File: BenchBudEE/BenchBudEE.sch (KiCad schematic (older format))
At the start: 0 parts

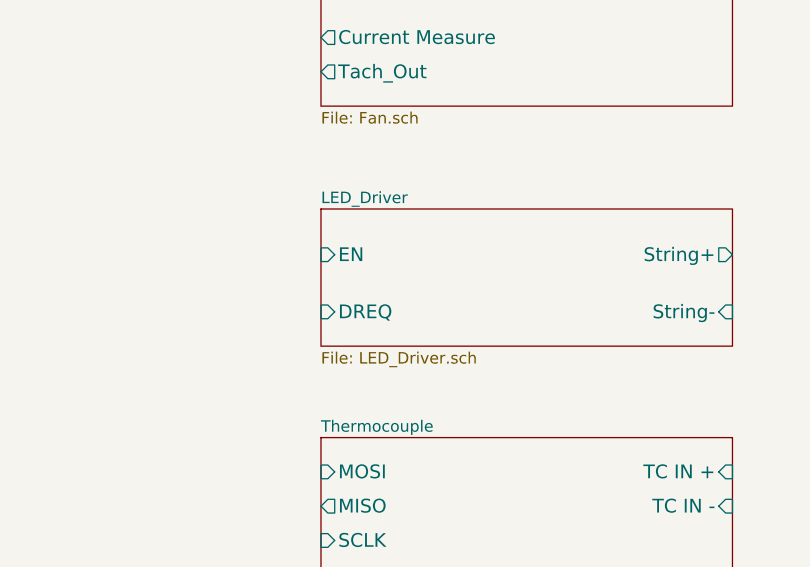
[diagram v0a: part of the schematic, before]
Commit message: Populated the LED Driver block based on the AP5726.
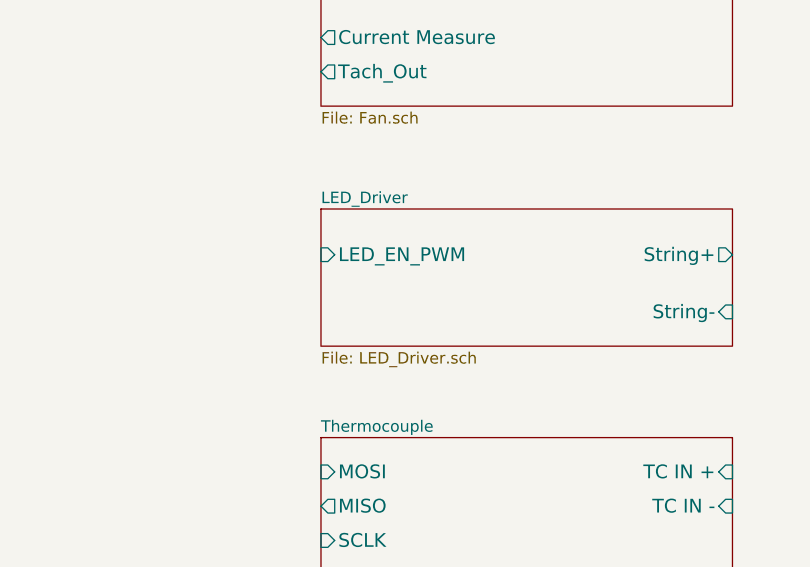
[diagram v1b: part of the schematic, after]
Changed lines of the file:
@@
 Sheet 1 9
 Title ""
-Date "9 feb 2014"
+Date "10 feb 2014"
 Rev ""
 Comp ""
@@
 F0 "LED_Driver" 50
 F1 "LED_Driver.sch" 50
-F2 "EN" I L 7850 4250 60
-F3 "DREQ" I L 7850 4500 60
-F4 "String+" O R 9650 4250 60
-F5 "String-" I R 9650 4500 60
+F2 "String+" O R 9650 4250 60
+F3 "String-" I R 9650 4500 60
+F4 "LED_EN_PWM" I L 7850 4250 60
 $EndSheet
 $Sheet

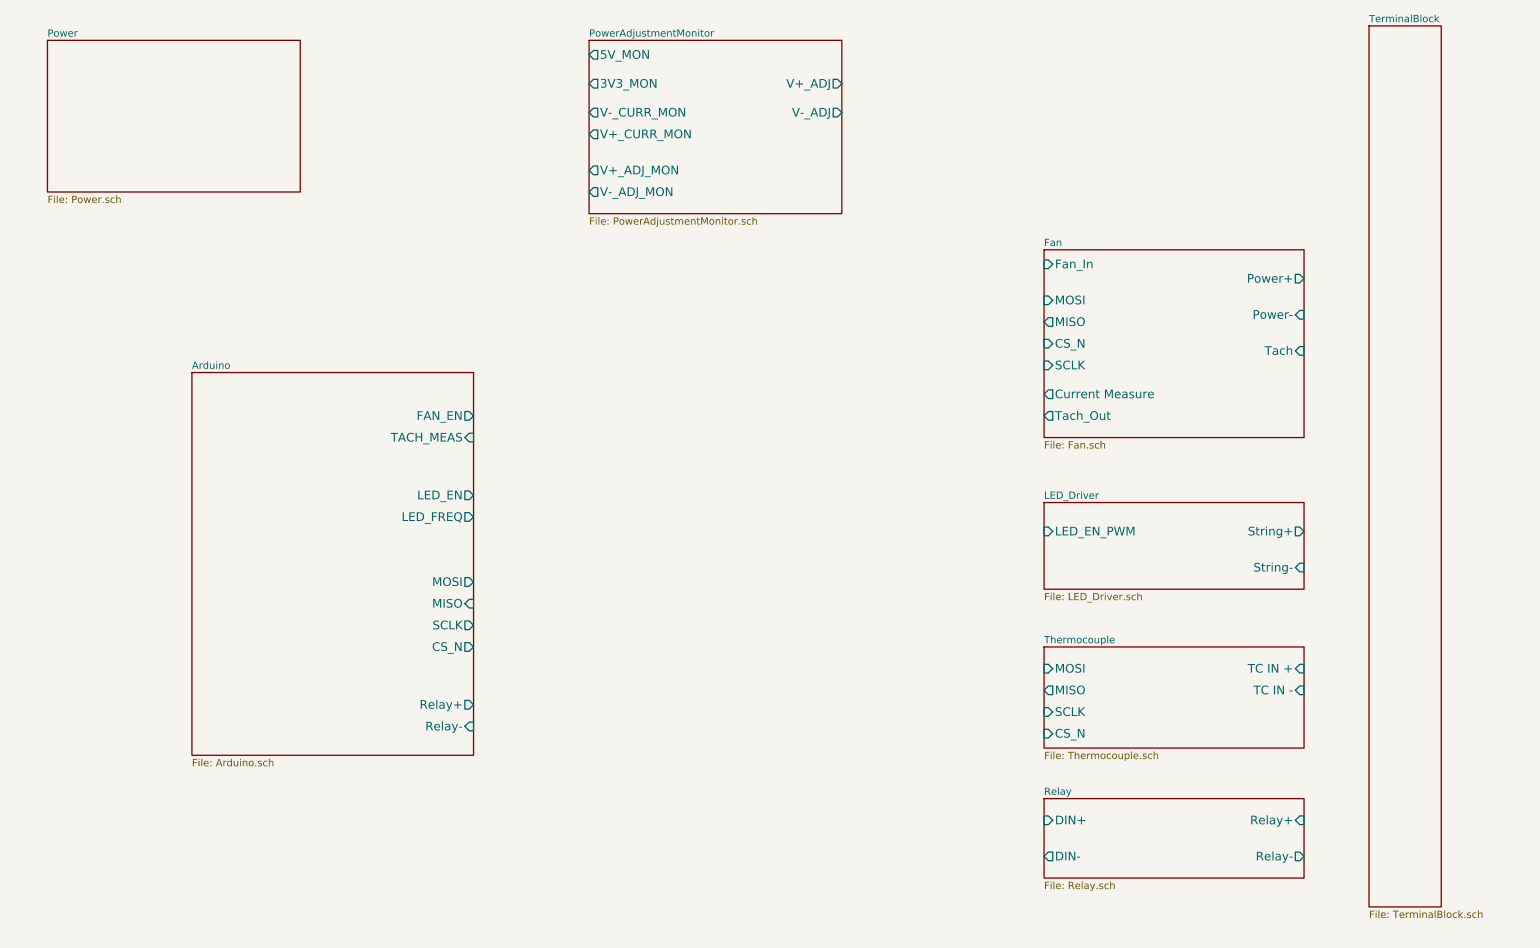
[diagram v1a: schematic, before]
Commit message: Populated the Arduino block and top level wiring.
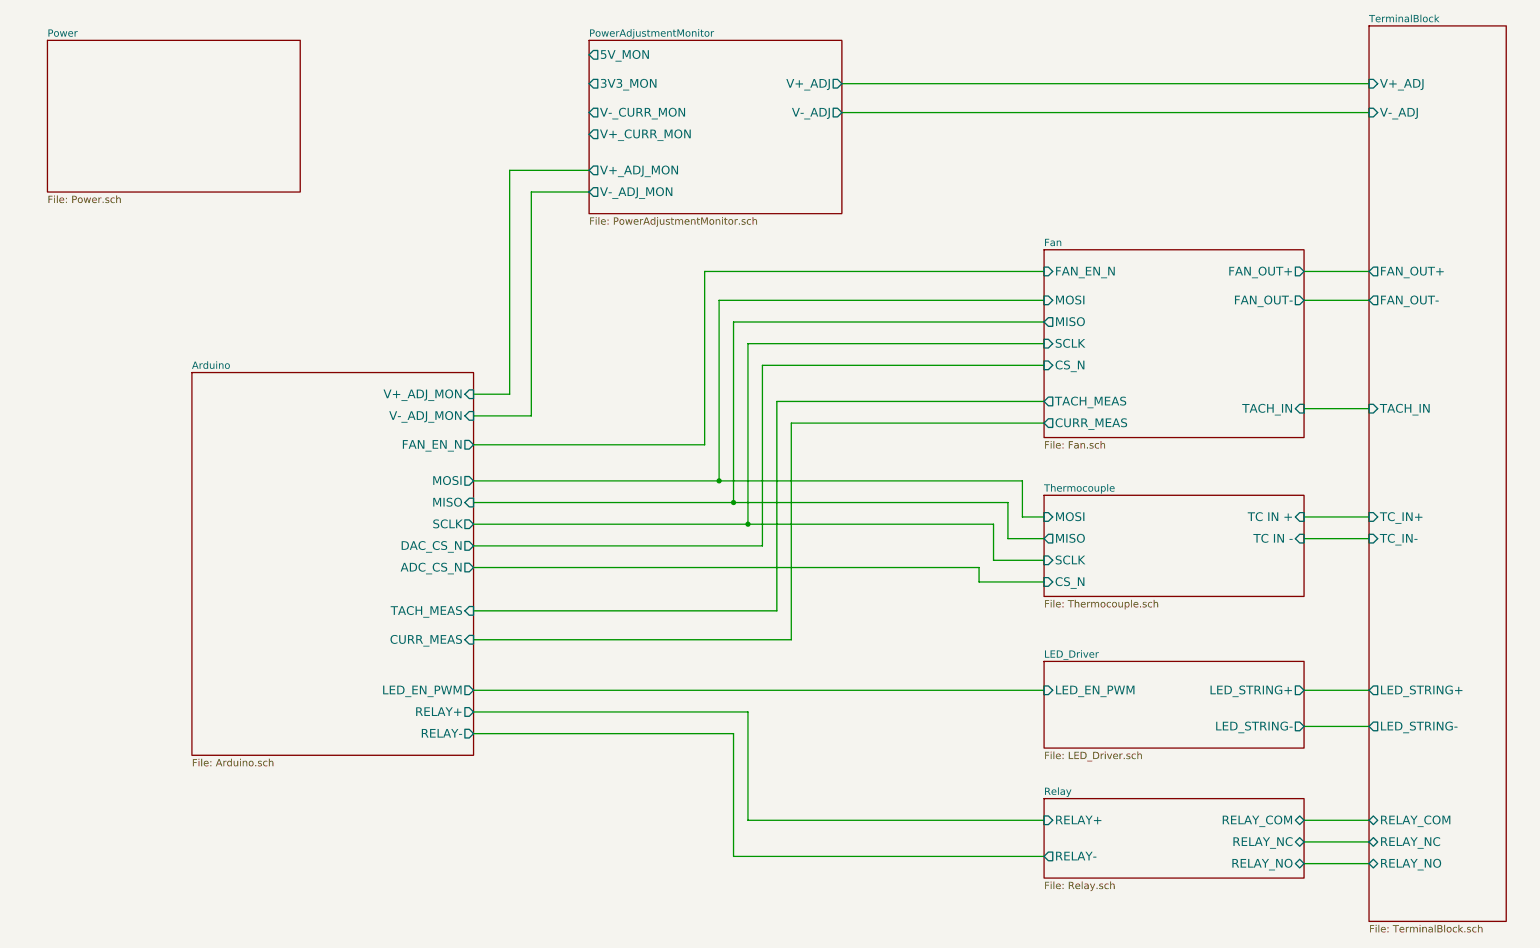
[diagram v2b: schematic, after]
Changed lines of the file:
@@
 $EndDescr
 $Sheet
-S 1950 3150 1950 2650
-U 52EC4D59
-F0 "Arduino" 50
-F1 "Arduino.sch" 50
-F2 "Relay+" O R 3900 5450 60
-F3 "Relay-" I R 3900 5600 60
-F4 "MOSI" O R 3900 4600 60
-F5 "MISO" I R 3900 4750 60
-F6 "SCLK" O R 3900 4900 60
-F7 "CS_N" O R 3900 5050 60
-F8 "LED_EN" O R 3900 4000 60
-F9 "LED_FREQ" O R 3900 4150 60
-F10 "FAN_EN" O R 3900 3450 60
-F11 "TACH_MEAS" I R 3900 3600 60
-$EndSheet
-$Sheet
-S 7850 5050 1800 700
+S 7850 4000 1800 700
 U 52EC4DA4
 F0 "Thermocouple" 50
 F1 "Thermocouple.sch" 50
-F2 "TC IN +" I R 9650 5200 60
-F3 "TC IN -" I R 9650 5350 60
-F4 "MOSI" I L 7850 5200 60
-F5 "MISO" O L 7850 5350 60
-F6 "SCLK" I L 7850 5500 60
-F7 "CS_N" I L 7850 5650 60
+F2 "TC IN +" I R 9650 4150 60
+F3 "TC IN -" I R 9650 4300 60
+F4 "MOSI" I L 7850 4150 60
+F5 "MISO" O L 7850 4300 60
+F6 "SCLK" I L 7850 4450 60
+F7 "CS_N" I L 7850 4600 60
 $EndSheet
 $Sheet
@@
 F0 "Relay" 50
 F1 "Relay.sch" 50
-F2 "DIN+" I L 7850 6250 60
-F3 "DIN-" O L 7850 6500 60
-F4 "Relay+" I R 9650 6250 60
-F5 "Relay-" O R 9650 6500 60
+F2 "RELAY_NC" B R 9650 6400 60
+F3 "RELAY_NO" B R 9650 6550 60
+F4 "RELAY_COM" B R 9650 6250 60
+F5 "RELAY+" I L 7850 6250 60
+F6 "RELAY-" O L 7850 6500 60
 $EndSheet
 $Sheet
@@
 $EndSheet
 $Sheet
-S 7850 4050 1800 600
+S 7850 5150 1800 600
 U 52EC4DEA
 F0 "LED_Driver" 50
 F1 "LED_Driver.sch" 50
-F2 "String+" O R 9650 4250 60
-F3 "String-" I R 9650 4500 60
-F4 "LED_EN_PWM" I L 7850 4250 60
-$EndSheet
-$Sheet
-S 10100 750  500  6100
-U 52EC4E3C
-F0 "TerminalBlock" 50
-F1 "TerminalBlock.sch" 50
+F2 "LED_EN_PWM" I L 7850 5350 60
+F3 "LED_STRING+" O R 9650 5350 60
+F4 "LED_STRING-" O R 9650 5600 60
 $EndSheet
 $Sheet
@@
 F0 "Fan" 50
 F1 "Fan.sch" 50
-F2 "Power+" O R 9650 2500 60
-F3 "Power-" I R 9650 2750 60
-F4 "Tach" I R 9650 3000 60
-F5 "Tach_Out" O L 7850 3450 60
-F6 "Fan_In" I L 7850 2400 60
-F7 "Current Measure" O L 7850 3300 60
-F8 "MOSI" I L 7850 2650 60
-F9 "MISO" O L 7850 2800 60
-F10 "CS_N" I L 7850 2950 60
-F11 "SCLK" I L 7850 3100 60
-$EndSheet
+F2 "MOSI" I L 7850 2650 60
+F3 "MISO" O L 7850 2800 60
+F4 "CS_N" I L 7850 3100 60
+F5 "SCLK" I L 7850 2950 60
+F6 "FAN_OUT+" O R 9650 2450 60
+F7 "TACH_IN" I R 9650 3400 60
+F8 "TACH_MEAS" O L 7850 3350 60
+F9 "FAN_EN_N" I L 7850 2450 60
+F10 "CURR_MEAS" O L 7850 3500 60
+F11 "FAN_OUT-" O R 9650 2650 60
+$EndSheet
+Wire Wire Line
+	10100 1150 6450 1150
+Wire Wire Line
+	10100 1350 6450 1350
+$Sheet
+S 10100 750  950  6200
+U 52EC4E3C
+F0 "TerminalBlock" 50
+F1 "TerminalBlock.sch" 50
+F2 "V+_ADJ" I L 10100 1150 60
+F3 "V-_ADJ" I L 10100 1350 60
+F4 "FAN_OUT+" O L 10100 2450 60
+F5 "FAN_OUT-" O L 10100 2650 60
+F6 "TACH_IN" I L 10100 3400 60
+F7 "LED_STRING+" O L 10100 5350 60
+F8 "LED_STRING-" O L 10100 5600 60
+F9 "TC_IN+" I L 10100 4150 60
+F10 "TC_IN-" I L 10100 4300 60
+F11 "RELAY_COM" B L 10100 6250 60
+F12 "RELAY_NO" B L 10100 6550 60
+F13 "RELAY_NC" B L 10100 6400 60
+$EndSheet
+Wire Wire Line
+	9650 2450 10100 2450
+Wire Wire Line
+	9650 2650 10100 2650
+Wire Wire Line
+	9650 3400 10100 3400
+Wire Wire Line
+	9650 6250 10100 6250
+Wire Wire Line
+	3900 3300 4150 3300
+Wire Wire Line
+	4150 3300 4150 1750
+Wire Wire Line
+	4150 1750 4700 1750
+Wire Wire Line
+	3900 3450 4300 3450
+Wire Wire Line
+	4300 3450 4300 1900
+Wire Wire Line
+	4300 1900 4700 1900
+$Sheet
+S 1950 3150 1950 2650
+U 52EC4D59
+F0 "Arduino" 50
+F1 "Arduino.sch" 50
+F2 "MOSI" O R 3900 3900 60
+F3 "MISO" I R 3900 4050 60
+F4 "SCLK" O R 3900 4200 60
+F5 "TACH_MEAS" I R 3900 4800 60
+F6 "RELAY+" O R 3900 5500 60
+F7 "RELAY-" O R 3900 5650 60
+F8 "FAN_EN_N" O R 3900 3650 60
+F9 "CURR_MEAS" I R 3900 5000 60
+F10 "V+_ADJ_MON" I R 3900 3300 60
+F11 "V-_ADJ_MON" I R 3900 3450 60
+F12 "LED_EN_PWM" O R 3900 5350 60
+F13 "DAC_CS_N" O R 3900 4350 60
+F14 "ADC_CS_N" O R 3900 4500 60
+$EndSheet
+Wire Wire Line
+	3900 3650 5500 3650
+Wire Wire Line
+	5500 3650 5500 2450
+Wire Wire Line
+	5500 2450 7850 2450
+Wire Wire Line
+	3900 3900 7700 3900
+Wire Wire Line
+	5600 3900 5600 2650
+Wire Wire Line
+	5600 2650 7850 2650
+Wire Wire Line
+	3900 4050 7600 4050
+Wire Wire Line
+	5700 4050 5700 2800
+Wire Wire Line
+	5700 2800 7850 2800
+Wire Wire Line
+	6000 3350 6000 4800
+Wire Wire Line
+	6000 3350 7850 3350
+Wire Wire Line
+	6100 3500 6100 5000
+Wire Wire Line
+	6100 3500 7850 3500
+Wire Wire Line
+	9650 4150 10100 4150
+Wire Wire Line
+	9650 4300 10100 4300
+Wire Wire Line
+	9650 5350 10100 5350
+Wire Wire Line
+	9650 5600 10100 5600
+Wire Wire Line
+	6100 5000 3900 5000
+Wire Wire Line
+	6000 4800 3900 4800
+Wire Wire Line
+	7850 2950 5800 2950
+Wire Wire Line
+	5800 2950 5800 4200
+Wire Wire Line
+	3900 4200 7500 4200
+Wire Wire Line
+	3900 4350 5900 4350
+Wire Wire Line
+	5900 4350 5900 3100
+Wire Wire Line
+	5900 3100 7850 3100
+Wire Wire Line
+	7850 4150 7700 4150
+Wire Wire Line
+	7700 4150 7700 3900
+Connection ~ 5600 3900
+Wire Wire Line
+	7850 4300 7600 4300
+Wire Wire Line
+	7600 4300 7600 4050
+Connection ~ 5700 4050
+Wire Wire Line
+	7850 4450 7500 4450
+Wire Wire Line
+	7500 4450 7500 4200
+Connection ~ 5800 4200
+Wire Wire Line
+	7850 4600 7400 4600
+Wire Wire Line
+	7400 4600 7400 4500
+Wire Wire Line
+	7400 4500 3900 4500
+Wire Wire Line
+	3900 5350 7850 5350
+Wire Wire Line
+	3900 5650 5700 5650
+Wire Wire Line
+	5700 5650 5700 6500
+Wire Wire Line
+	5700 6500 7850 6500
+Wire Wire Line
+	3900 5500 5800 5500
+Wire Wire Line
+	5800 5500 5800 6250
+Wire Wire Line
+	5800 6250 7850 6250
+Wire Wire Line
+	9650 6400 10100 6400
+Wire Wire Line
+	9650 6550 10100 6550
 $EndSCHEMATC

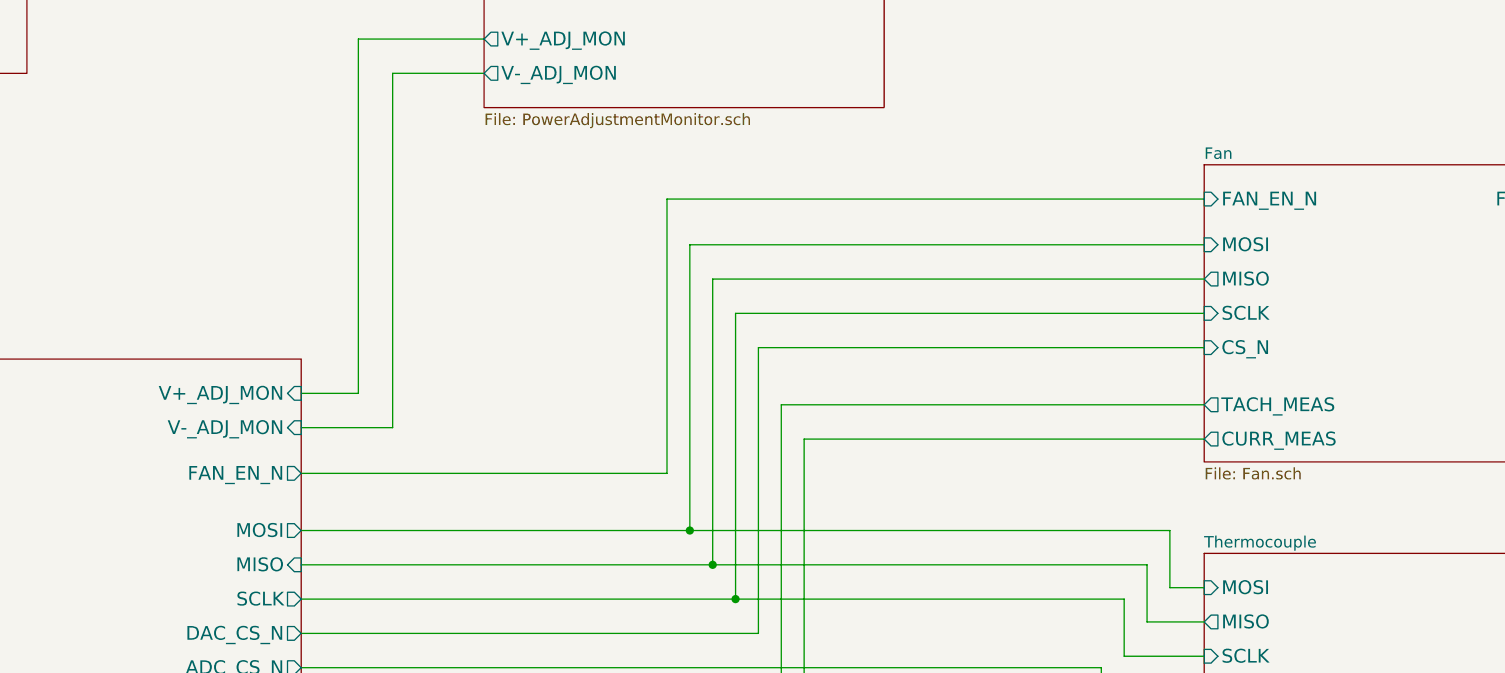
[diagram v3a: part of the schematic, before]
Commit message: Current/fan module refactoring.
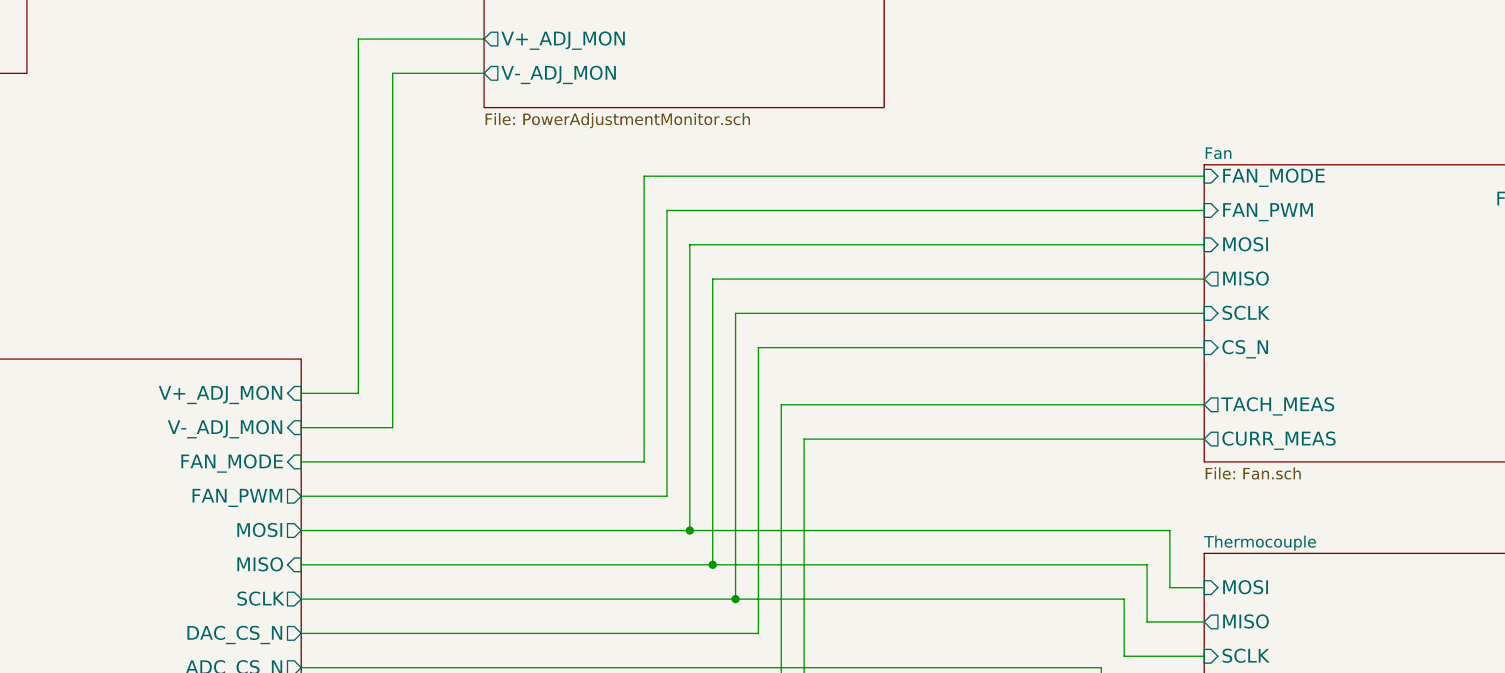
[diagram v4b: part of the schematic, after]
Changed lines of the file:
@@
 F7 "TACH_IN" I R 9650 3400 60
 F8 "TACH_MEAS" O L 7850 3350 60
-F9 "FAN_EN_N" I L 7850 2450 60
-F10 "CURR_MEAS" O L 7850 3500 60
-F11 "FAN_OUT-" O R 9650 2650 60
+F9 "CURR_MEAS" O L 7850 3500 60
+F10 "FAN_OUT-" O R 9650 2650 60
+F11 "FAN_PWM" I L 7850 2500 60
+F12 "FAN_MODE" I L 7850 2350 60
 $EndSheet
 Wire Wire Line
@@
 F6 "RELAY+" O R 3900 5500 60
 F7 "RELAY-" O R 3900 5650 60
-F8 "FAN_EN_N" O R 3900 3650 60
-F9 "CURR_MEAS" I R 3900 5000 60
-F10 "V+_ADJ_MON" I R 3900 3300 60
-F11 "V-_ADJ_MON" I R 3900 3450 60
-F12 "LED_EN_PWM" O R 3900 5350 60
-F13 "DAC_CS_N" O R 3900 4350 60
-F14 "ADC_CS_N" O R 3900 4500 60
+F8 "CURR_MEAS" I R 3900 5000 60
+F9 "V+_ADJ_MON" I R 3900 3300 60
+F10 "V-_ADJ_MON" I R 3900 3450 60
+F11 "LED_EN_PWM" O R 3900 5350 60
+F12 "DAC_CS_N" O R 3900 4350 60
+F13 "ADC_CS_N" O R 3900 4500 60
+F14 "FAN_PWM" O R 3900 3750 60
+F15 "FAN_MODE" I R 3900 3600 60
 $EndSheet
 Wire Wire Line
-	3900 3650 5500 3650
-Wire Wire Line
-	5500 3650 5500 2450
-Wire Wire Line
-	5500 2450 7850 2450
+	3900 3750 5500 3750
 Wire Wire Line
 	3900 3900 7700 3900
@@
 Wire Wire Line
 	9650 6550 10100 6550
+Wire Wire Line
+	5500 3750 5500 2500
+Wire Wire Line
+	5500 2500 7850 2500
+Wire Wire Line
+	7850 2350 5400 2350
+Wire Wire Line
+	5400 2350 5400 3600
+Wire Wire Line
+	5400 3600 3900 3600
 $EndSCHEMATC

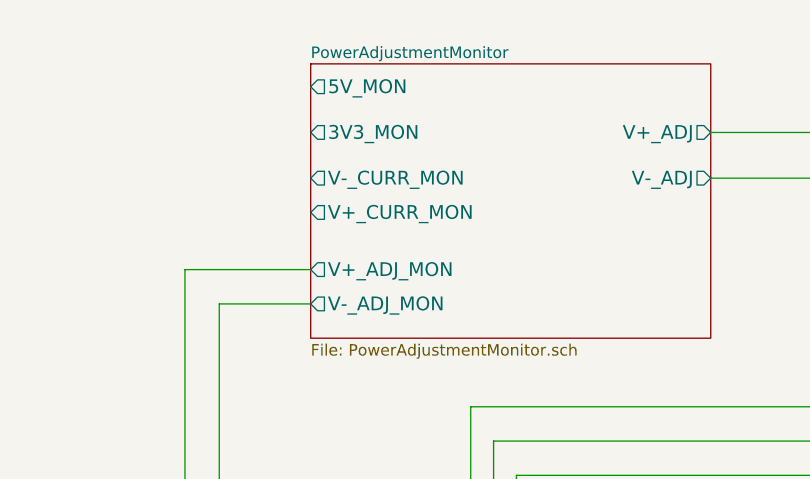
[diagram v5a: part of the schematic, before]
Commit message: Connected Arduino power/ground. +5V power filtering. Removed current monitoring.
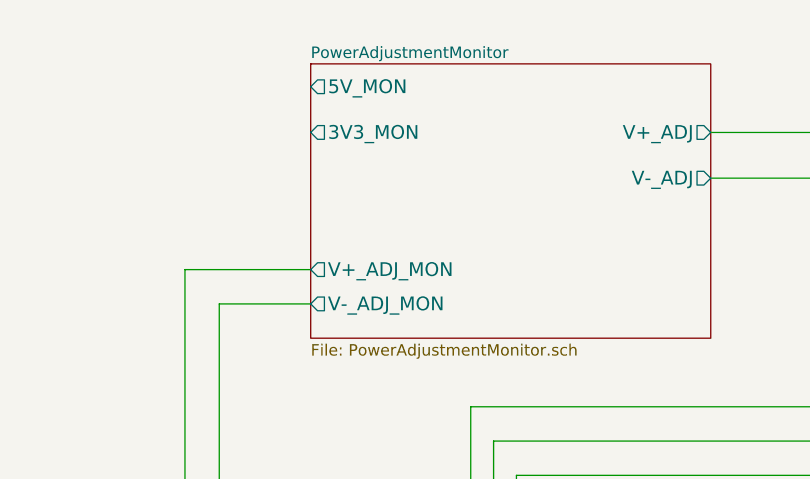
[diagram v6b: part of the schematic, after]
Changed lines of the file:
@@
 Sheet 1 9
 Title ""
-Date "14 feb 2014"
+Date "19 feb 2014"
 Rev ""
 Comp ""
@@
 F6 "V+_ADJ_MON" O L 4700 1750 60
 F7 "V-_ADJ_MON" O L 4700 1900 60
-F8 "V-_CURR_MON" O L 4700 1350 60
-F9 "V+_CURR_MON" O L 4700 1500 60
 $EndSheet
 $Sheet
